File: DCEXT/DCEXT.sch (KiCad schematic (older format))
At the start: 20 parts, among them J1 SPK_L, J2 SPK_R, J3 USB1015-XX-X-X_REVC, J4 USB1015-XX-X-X_REVC, J5 FAN_CON, J6 Conn_02x17_Odd_Even, Q1 SI2310, U1 MPCIE-Socket, U2 USBUF02W6, U3 USBUF02W6

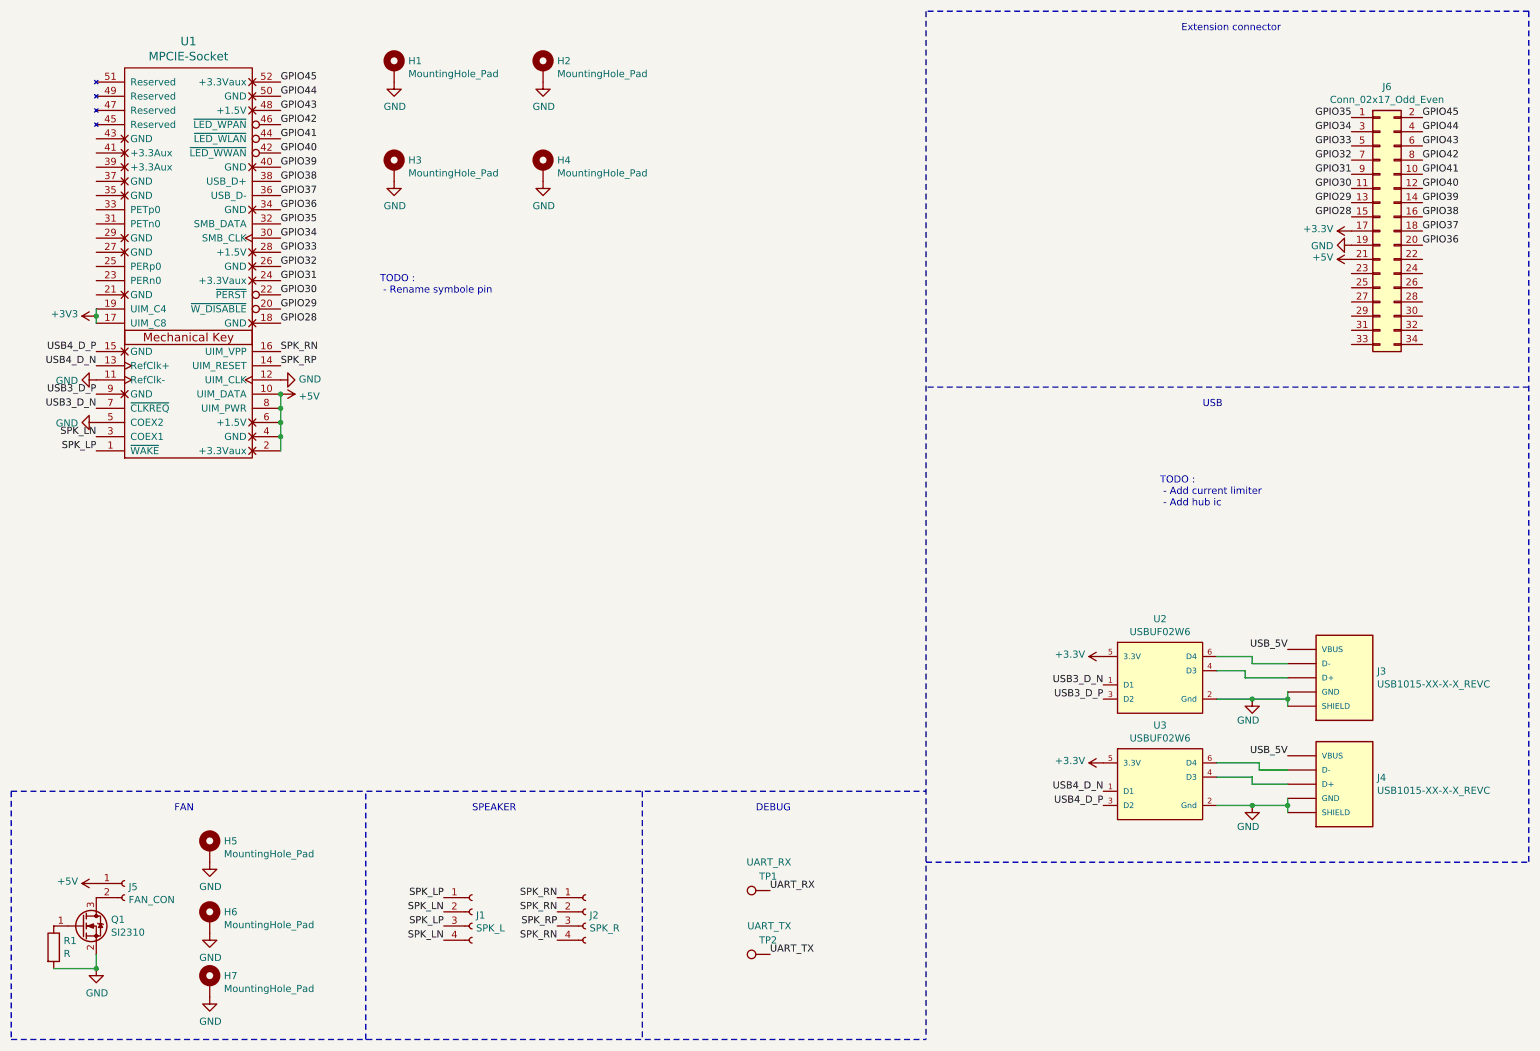
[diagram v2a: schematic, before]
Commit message: Fix usb position,holes and pcb outline, add current limiter
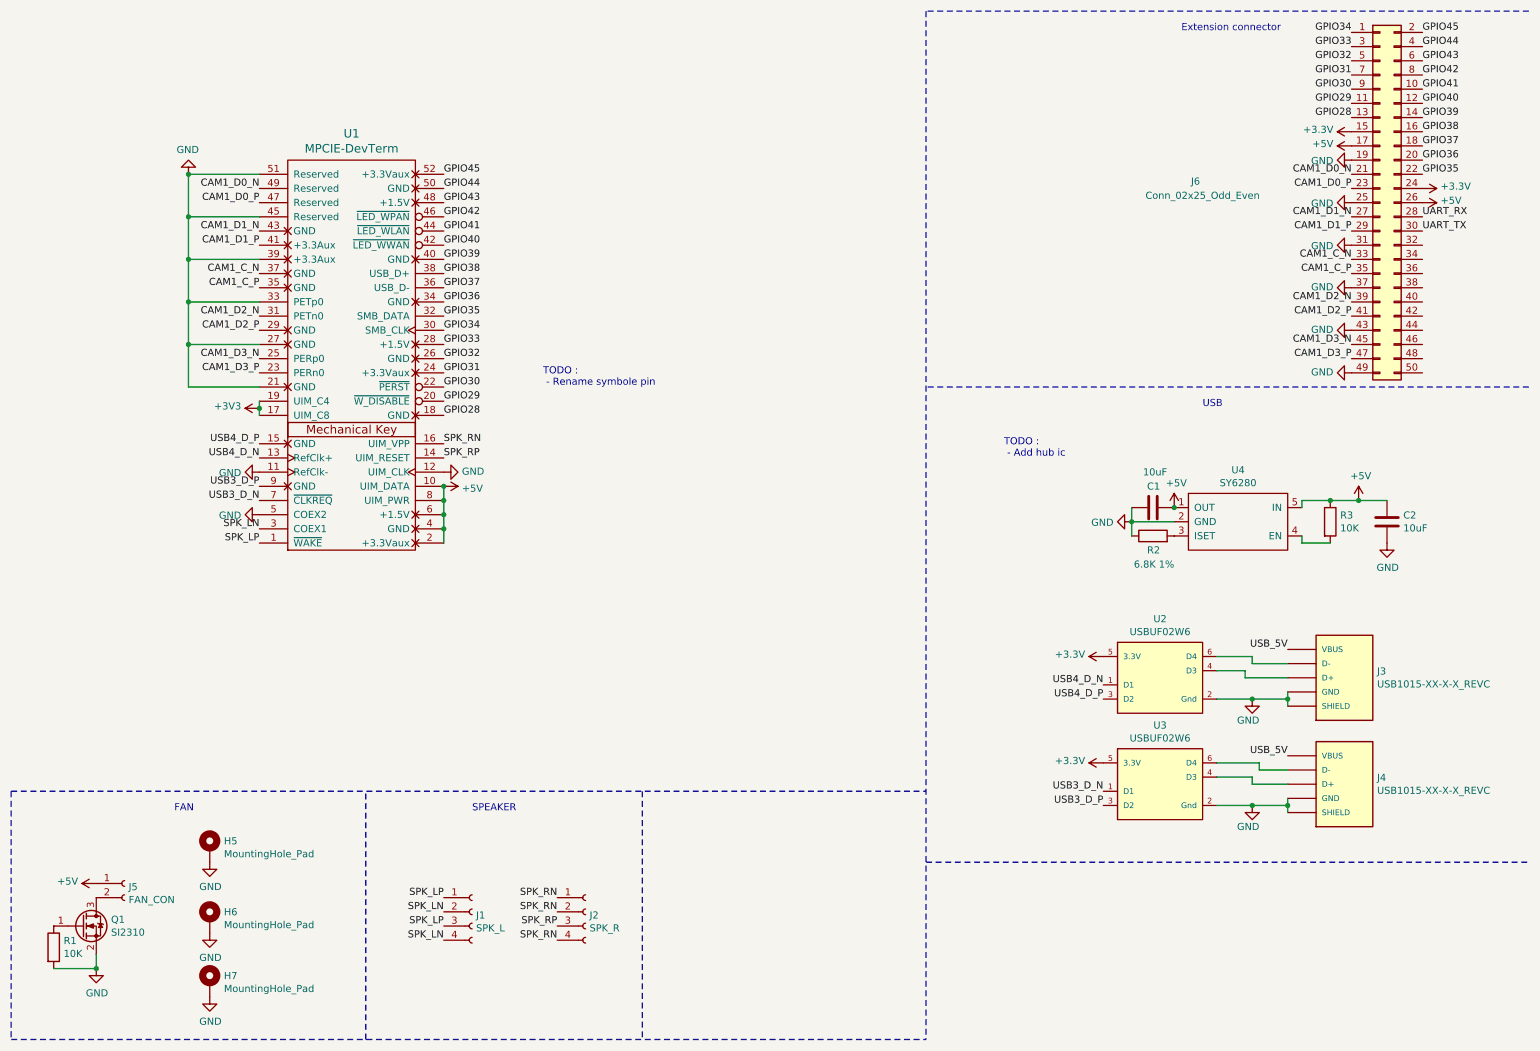
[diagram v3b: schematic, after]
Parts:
- removed H1, H2, H3, H4: MountingHole_Pad, MountingHole:MountingHole_5mm_Pad_TopBottom, symbol Mechanical:MountingHole_Pad
- removed J6: Conn_02x17_Odd_Even, Connector_FFC-FPC:Hirose_FH12-34S-0.5SH_1x34-1MP_P0.50mm_Horizontal, symbol Connector_Generic:Conn_02x17_Odd_Even
- removed TP1: UART_RX, TestPoint:TestPoint_Pad_D2.5mm, symbol Connector:TestPoint
- removed TP2: UART_TX, TestPoint:TestPoint_Pad_D2.5mm, symbol Connector:TestPoint
- removed U1: MPCIE-Socket, mpcie:devtermMPCIE, symbol mpcie:MPCIE-Socket
- added C1, C2: 10uF, Capacitor_SMD:C_0402_1005Metric_Pad0.74x0.62mm_HandSolder, symbol Device:C
- added J6: Conn_02x25_Odd_Even, Connector_FFC-FPC:Hirose_FH12-50S-0.5SH_1x50-1MP_P0.50mm_Horizontal, symbol Connector_Generic:Conn_02x25_Odd_Even
- added R2: 6.8K 1%, Resistor_SMD:R_0402_1005Metric_Pad0.72x0.64mm_HandSolder, symbol Device:R
- added R3: 10K, Resistor_SMD:R_0402_1005Metric_Pad0.72x0.64mm_HandSolder, symbol Device:R
- added U1: MPCIE-DevTerm, mpcie:devtermMPCIE, symbol mpcie:MPCIE-DevTerm
- added U4: SY6280, Package_TO_SOT_SMD:SOT-23-5_HandSoldering, symbol myLib:SY6280
- R1: value R -> 10K
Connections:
- net +3V3: now also J6.15 (Pin_15), J6.24 (Pin_24), U1.17 (UIM_C8), U1.19 (UIM_C4)
- net +5V: now also C1.2, C2.1, J6.17 (Pin_17), J6.26 (Pin_26), R3.1, U1.10 (UIM_DATA), U1.2 (+3.3Vaux), U1.4 (GND), U1.6 (+1.5V), U1.8 (UIM_PWR), U4.1 (OUT), U4.5 (IN)
- net GND: now also C1.1, C2.2, J6.19 (Pin_19), J6.25 (Pin_25), J6.31 (Pin_31), J6.37 (Pin_37), J6.43 (Pin_43), J6.49 (Pin_49), R2.1, U1.11 (RefClk-), U1.12 (UIM_CLK), U1.21 (GND), U1.27 (GND), U1.33 (PETp0), U1.39 (+3.3Aux), U1.45 (Reserved), U1.5 (COEX2), U1.51 (Reserved), U4.2 (GND)
- net GPIO28: now also J6.13 (Pin_13), U1.18 (GND)
- net GPIO29: now also J6.11 (Pin_11), U1.20 (~W_DISABLE)
- net GPIO30: now also J6.9 (Pin_9), U1.22 (~PERST)
- net GPIO31: now also J6.7 (Pin_7), U1.24 (+3.3Vaux)
- net GPIO32: now also J6.5 (Pin_5), U1.26 (GND)
- net GPIO33: now also J6.3 (Pin_3), U1.28 (+1.5V)
- net GPIO34: now also J6.1 (Pin_1), U1.30 (SMB_CLK)
- net GPIO35: now also J6.22 (Pin_22), U1.32 (SMB_DATA)
- net GPIO36: now also J6.20 (Pin_20), U1.34 (GND)
- net GPIO37: now also J6.18 (Pin_18), U1.36 (USB_D-)
- net GPIO38: now also J6.16 (Pin_16), U1.38 (USB_D+)
- net GPIO39: now also J6.14 (Pin_14), U1.40 (GND)
- net GPIO40: now also J6.12 (Pin_12), U1.42 (~LED_WWAN)
- net GPIO41: now also J6.10 (Pin_10), U1.44 (~LED_WLAN)
- net GPIO42: now also J6.8 (Pin_8), U1.46 (~LED_WPAN)
- net GPIO43: now also J6.6 (Pin_6), U1.48 (+1.5V)
- net GPIO44: now also J6.4 (Pin_4), U1.50 (GND)
- net GPIO45: now also J6.2 (Pin_2), U1.52 (+3.3Vaux)
- net SPK_LN: now also U1.3 (COEX1)
- net SPK_LP: now also U1.1 (~WAKE)
- net SPK_RN: now also U1.16 (UIM_VPP)
- net SPK_RP: now also U1.14 (UIM_RESET)
- net UART_RX: now also J6.28 (Pin_28)
- net UART_TX: now also J6.30 (Pin_30)
- net USB3_D_N: now also U3.1 (D1), U1.7 (~CLKREQ); no longer U2.1 (D1)
- net USB3_D_P: now also U3.3 (D2), U1.9 (GND); no longer U2.3 (D2)
- net USB4_D_N: now also U2.1 (D1), U1.13 (RefClk+); no longer U3.1 (D1)
- net USB4_D_P: now also U2.3 (D2), U1.15 (GND); no longer U3.3 (D2)
- new net: R2.2, U4.3 (ISET)
- new net: R3.2, U4.4 (EN)
- new net CAM1_C_N: J6.33 (Pin_33), U1.37 (GND)
- new net CAM1_C_P: J6.35 (Pin_35), U1.35 (GND)
- new net CAM1_D0_N: J6.21 (Pin_21), U1.49 (Reserved)
- new net CAM1_D0_P: J6.23 (Pin_23), U1.47 (Reserved)
- new net CAM1_D1_N: J6.27 (Pin_27), U1.43 (GND)
- new net CAM1_D1_P: J6.29 (Pin_29), U1.41 (+3.3Aux)
- new net CAM1_D2_N: J6.39 (Pin_39), U1.31 (PETn0)
- new net CAM1_D2_P: J6.41 (Pin_41), U1.29 (GND)
- new net CAM1_D3_N: J6.45 (Pin_45), U1.25 (PERp0)
- new net CAM1_D3_P: J6.47 (Pin_47), U1.23 (PERn0)
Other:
- note added: "TODO :\n - Add hub ic"
- note removed: "DEBUG"
- note removed: "TODO :\n - Add current limiter\n - Add hub ic"

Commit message: Progess
Pop OS and kicad decided i didnt need 3d acceleration anymore, switching to mac
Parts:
- removed H5, H6, H7: MountingHole_Pad, MountingHole:MountingHole_2.2mm_M2_DIN965_Pad_TopBottom, symbol Mechanical:MountingHole_Pad
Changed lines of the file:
@@
 	0    -1   -1   0
-$EndComp
-$Comp
-L Mechanical:MountingHole_Pad H6
-U 1 1 61400A5B
-P 1900 6900
-F 0 "H6" H 2000 6949 50  0000 L CNN
-F 1 "MountingHole_Pad" H 2000 6858 50  0000 L CNN
-F 2 "MountingHole:MountingHole_2.2mm_M2_DIN965_Pad_TopBottom" H 1900 6900 50  0001 C CNN
-F 3 "~" H 1900 6900 50  0001 C CNN
-	1    1900 6900
-	1    0    0    -1
-$EndComp
-$Comp
-L power:GND #PWR0107
-U 1 1 61401B17
-P 1900 7000
-F 0 "#PWR0107" H 1900 6750 50  0001 C CNN
-F 1 "GND" H 1905 6827 50  0000 C CNN
-F 2 "" H 1900 7000 50  0001 C CNN
-F 3 "" H 1900 7000 50  0001 C CNN
-	1    1900 7000
-	1    0    0    -1
-$EndComp
-$Comp
-L Mechanical:MountingHole_Pad H7
-U 1 1 61402FE4
-P 1900 7350
-F 0 "H7" H 2000 7399 50  0000 L CNN
-F 1 "MountingHole_Pad" H 2000 7308 50  0000 L CNN
-F 2 "MountingHole:MountingHole_2.2mm_M2_DIN965_Pad_TopBottom" H 1900 7350 50  0001 C CNN
-F 3 "~" H 1900 7350 50  0001 C CNN
-	1    1900 7350
-	1    0    0    -1
-$EndComp
-$Comp
-L power:GND #PWR0108
-U 1 1 61402FEA
-P 1900 7450
-F 0 "#PWR0108" H 1900 7200 50  0001 C CNN
-F 1 "GND" H 1905 7277 50  0000 C CNN
-F 2 "" H 1900 7450 50  0001 C CNN
-F 3 "" H 1900 7450 50  0001 C CNN
-	1    1900 7450
-	1    0    0    -1
-$EndComp
-$Comp
-L Mechanical:MountingHole_Pad H5
-U 1 1 61408F3A
-P 1900 6400
-F 0 "H5" H 2000 6449 50  0000 L CNN
-F 1 "MountingHole_Pad" H 2000 6358 50  0000 L CNN
-F 2 "MountingHole:MountingHole_2.2mm_M2_DIN965_Pad_TopBottom" H 1900 6400 50  0001 C CNN
-F 3 "~" H 1900 6400 50  0001 C CNN
-	1    1900 6400
-	1    0    0    -1
-$EndComp
-$Comp
-L power:GND #PWR0109
-U 1 1 61408F40
-P 1900 6500
-F 0 "#PWR0109" H 1900 6250 50  0001 C CNN
-F 1 "GND" H 1905 6327 50  0000 C CNN
-F 2 "" H 1900 6500 50  0001 C CNN
-F 3 "" H 1900 6500 50  0001 C CNN
-	1    1900 6500
-	1    0    0    -1
 $EndComp
 Wire Notes Line

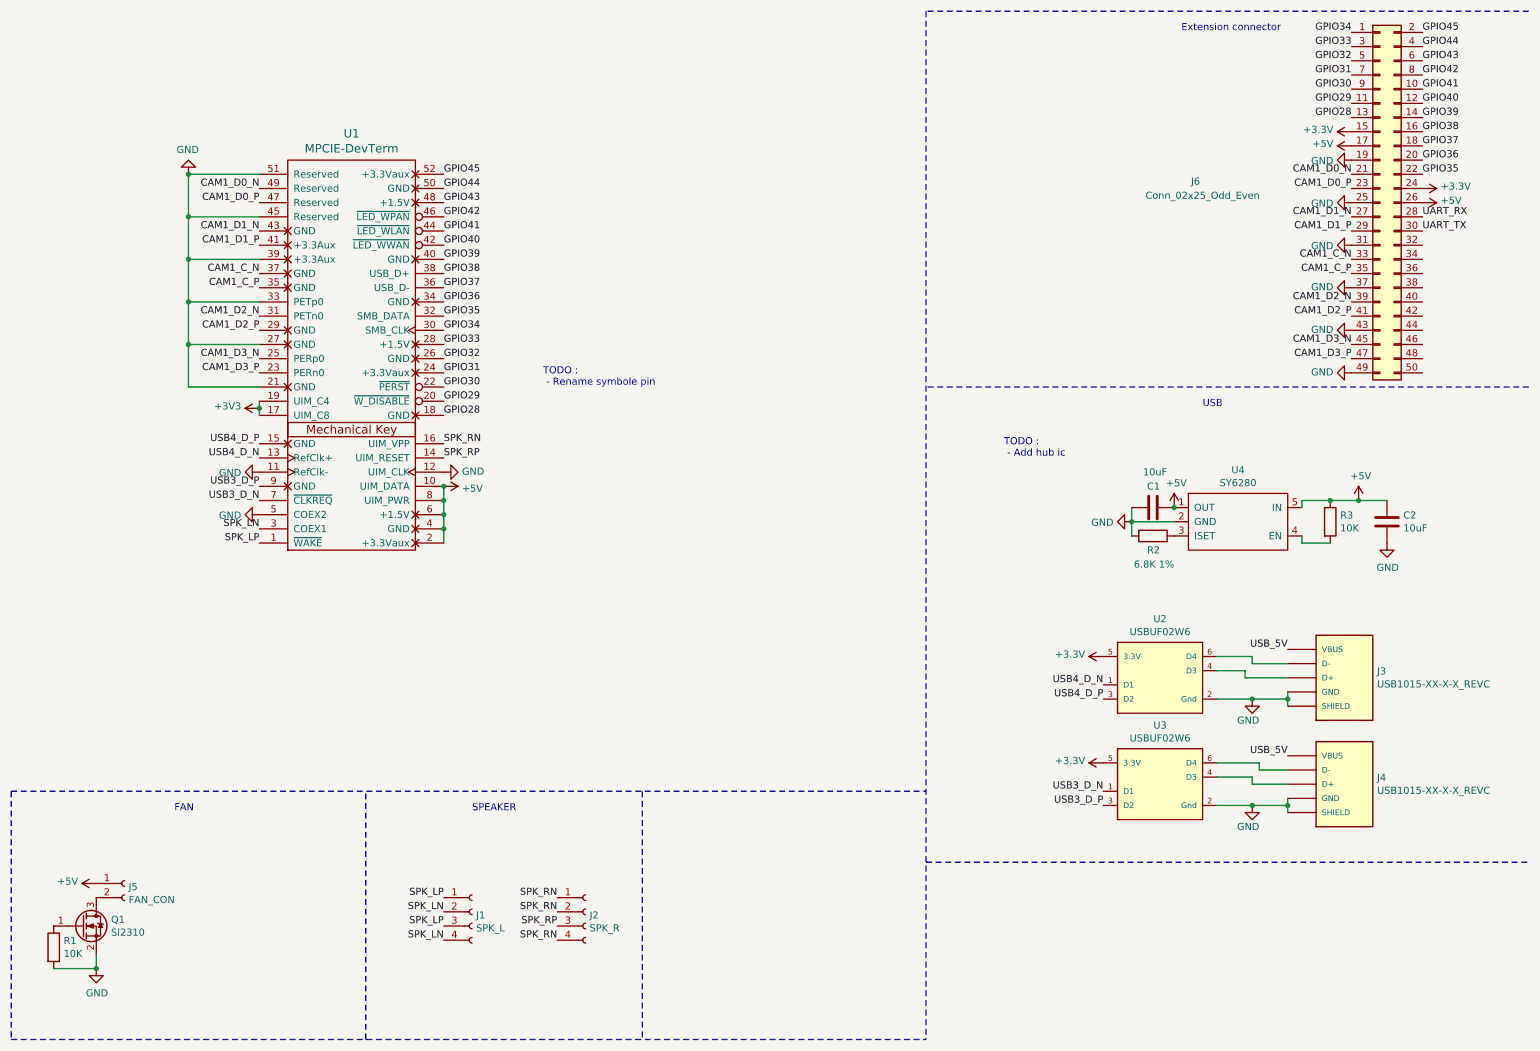
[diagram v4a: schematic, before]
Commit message: Fix usb position (for the last time !), speaker connector and routing
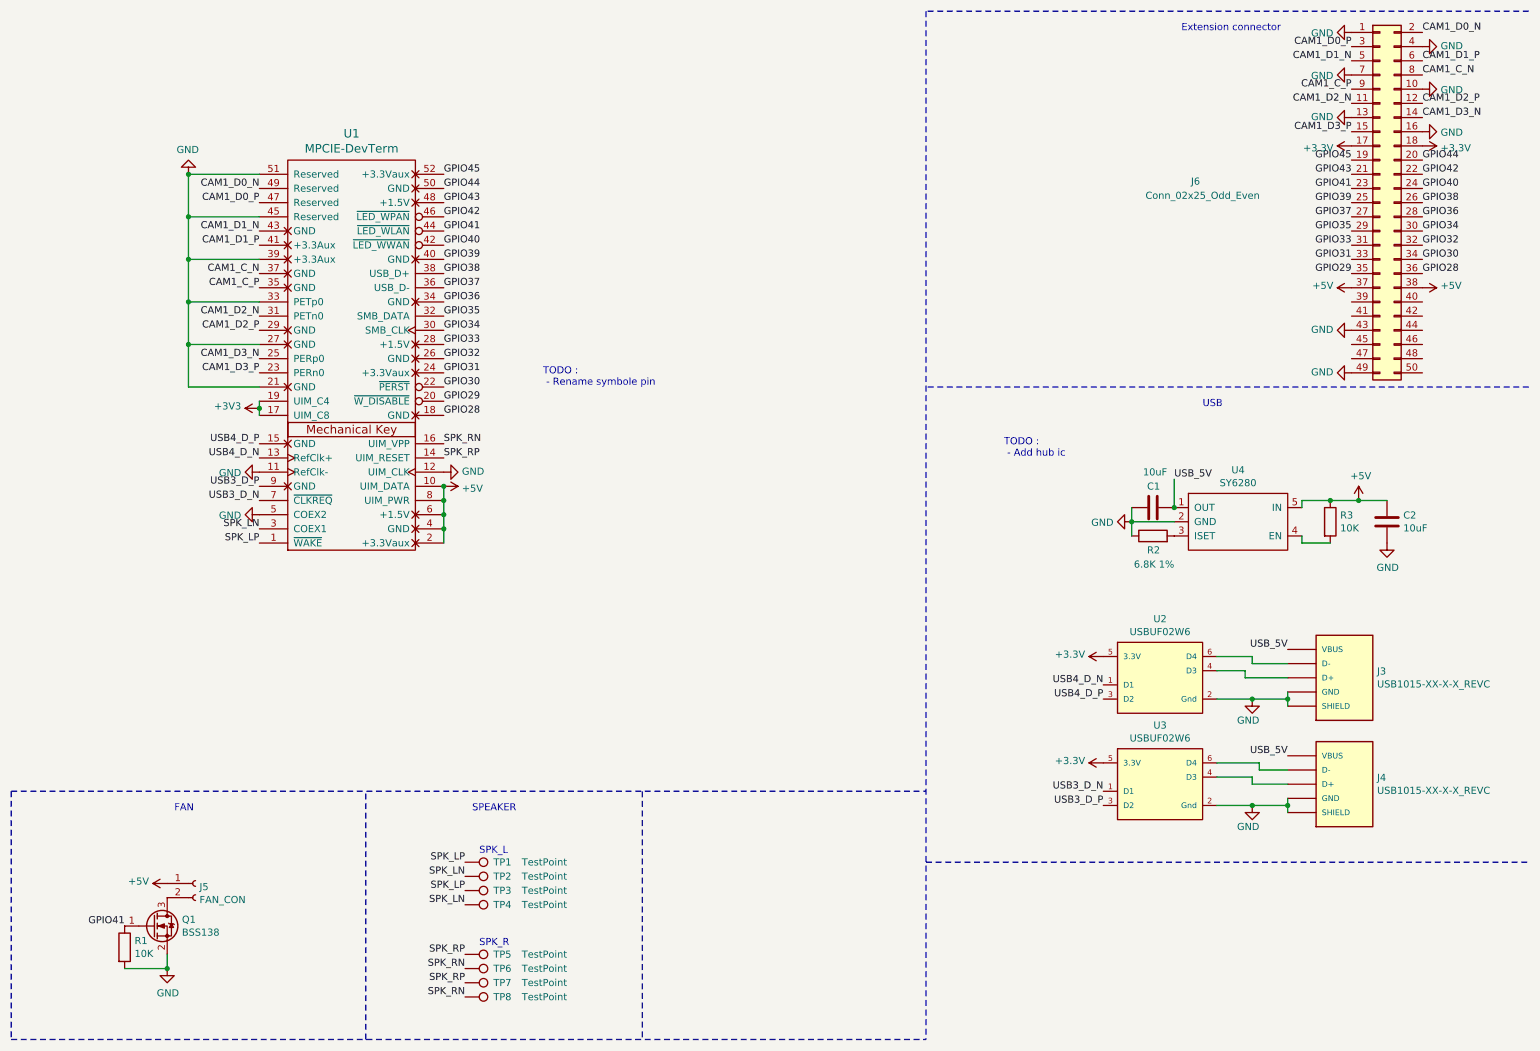
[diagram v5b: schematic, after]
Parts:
- removed J1: SPK_L, symbol Connector:Conn_01x04_Female
- removed J2: SPK_R, symbol Connector:Conn_01x04_Female
- removed Q1: SI2310, Package_TO_SOT_SMD:SOT-23, symbol Transistor_FET:2N7002
- added Q1: BSS138, Package_TO_SOT_SMD:SOT-23, symbol Transistor_FET:BSS138
- added TP1, TP2, TP3, TP4, TP5, TP6, TP7, TP8: TestPoint, TestPoint:TestPoint_Pad_3.0x3.0mm, symbol Connector:TestPoint
- J5: footprint (none) -> Connector_JST:JST_PH_S2B-PH-K_1x02_P2.00mm_Horizontal
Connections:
- net UART_RX is gone; now on net GPIO36: J6.28 (Pin_28)
- net UART_TX is gone; now on net GPIO34: J6.30 (Pin_30)
- net +3V3: now also J6.17 (Pin_17), J6.18 (Pin_18); no longer J6.15 (Pin_15), J6.24 (Pin_24)
- net +5V: now also J6.37 (Pin_37), J6.38 (Pin_38); no longer C1.2, J6.17 (Pin_17), J6.26 (Pin_26), U4.1 (OUT)
- net CAM1_C_N: now also J6.8 (Pin_8); no longer J6.33 (Pin_33)
- net CAM1_C_P: now also J6.9 (Pin_9); no longer J6.35 (Pin_35)
- net CAM1_D0_N: now also J6.2 (Pin_2); no longer J6.21 (Pin_21)
- net CAM1_D0_P: now also J6.3 (Pin_3); no longer J6.23 (Pin_23)
- net CAM1_D1_N: now also J6.5 (Pin_5); no longer J6.27 (Pin_27)
- net CAM1_D1_P: now also J6.6 (Pin_6); no longer J6.29 (Pin_29)
- net CAM1_D2_N: now also J6.11 (Pin_11); no longer J6.39 (Pin_39)
- net CAM1_D2_P: now also J6.12 (Pin_12); no longer J6.41 (Pin_41)
- net CAM1_D3_N: now also J6.14 (Pin_14); no longer J6.45 (Pin_45)
- net CAM1_D3_P: now also J6.15 (Pin_15); no longer J6.47 (Pin_47)
- net GND: now also J6.1 (Pin_1), J6.10 (Pin_10), J6.13 (Pin_13), J6.16 (Pin_16), J6.4 (Pin_4), J6.7 (Pin_7), Q1.2 (S); no longer J6.19 (Pin_19), J6.25 (Pin_25), J6.31 (Pin_31), J6.37 (Pin_37)
- net GPIO28: now also J6.36 (Pin_36); no longer J6.13 (Pin_13)
- net GPIO29: now also J6.35 (Pin_35); no longer J6.11 (Pin_11)
- net GPIO30: now also J6.34 (Pin_34); no longer J6.9 (Pin_9)
- net GPIO31: now also J6.33 (Pin_33); no longer J6.7 (Pin_7)
- net GPIO32: now also J6.32 (Pin_32); no longer J6.5 (Pin_5)
- net GPIO33: now also J6.31 (Pin_31); no longer J6.3 (Pin_3)
- net GPIO34: no longer J6.1 (Pin_1)
- net GPIO35: now also J6.29 (Pin_29); no longer J6.22 (Pin_22)
- net GPIO36: no longer J6.20 (Pin_20)
- net GPIO37: now also J6.27 (Pin_27); no longer J6.18 (Pin_18)
- net GPIO38: now also J6.26 (Pin_26); no longer J6.16 (Pin_16)
- net GPIO39: now also J6.25 (Pin_25); no longer J6.14 (Pin_14)
- net GPIO40: now also J6.24 (Pin_24); no longer J6.12 (Pin_12)
- net GPIO41: now also J6.23 (Pin_23), R1.1, Q1.1 (G); no longer J6.10 (Pin_10)
- net GPIO42: now also J6.22 (Pin_22); no longer J6.8 (Pin_8)
- net GPIO43: now also J6.21 (Pin_21); no longer J6.6 (Pin_6)
- net GPIO44: now also J6.20 (Pin_20); no longer J6.4 (Pin_4)
- net GPIO45: now also J6.19 (Pin_19); no longer J6.2 (Pin_2)
- net SPK_LN: now also TP2.1, TP4.1
- net SPK_LP: now also TP1.1, TP3.1
- net SPK_RN: now also TP6.1, TP8.1
- net SPK_RP: now also TP5.1, TP7.1
- net USB_5V: now also C1.2, U4.1 (OUT)
- net at J5.2 (Pin_2): now also Q1.3 (D)
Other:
- note added: "SPK_L"
- note added: "SPK_R"
- moved on the sheet: J5, R1
